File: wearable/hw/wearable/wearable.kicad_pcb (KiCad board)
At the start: 2 copper layers, 80.5 x 35.5 mm, 112 parts, among them IC1 LM4041CILPR, J2 Conn_02x05_Odd_Even, J8 USBC Charger, SW1 SW_Toggle, U1 LT3042xMSE, U2 BNO080, U3 nRF54L15-QFXX, U4 TPS61040DBV, U5 ADS1299IPAG, U6 nPM1300-QEXX, Y1 32MHz, Y2 32.768kHz, Y3 32.768kHz

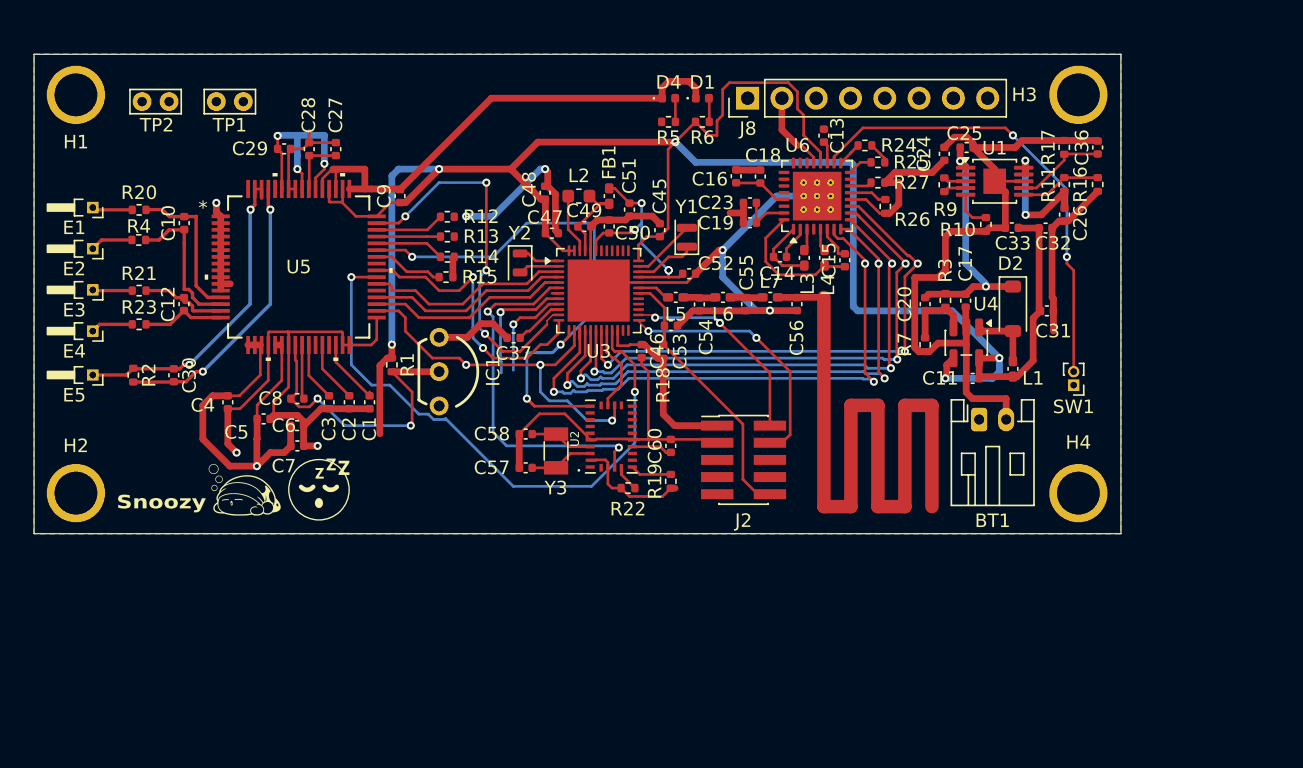
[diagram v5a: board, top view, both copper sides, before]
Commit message: Finished routing (mostly) + better testpoints
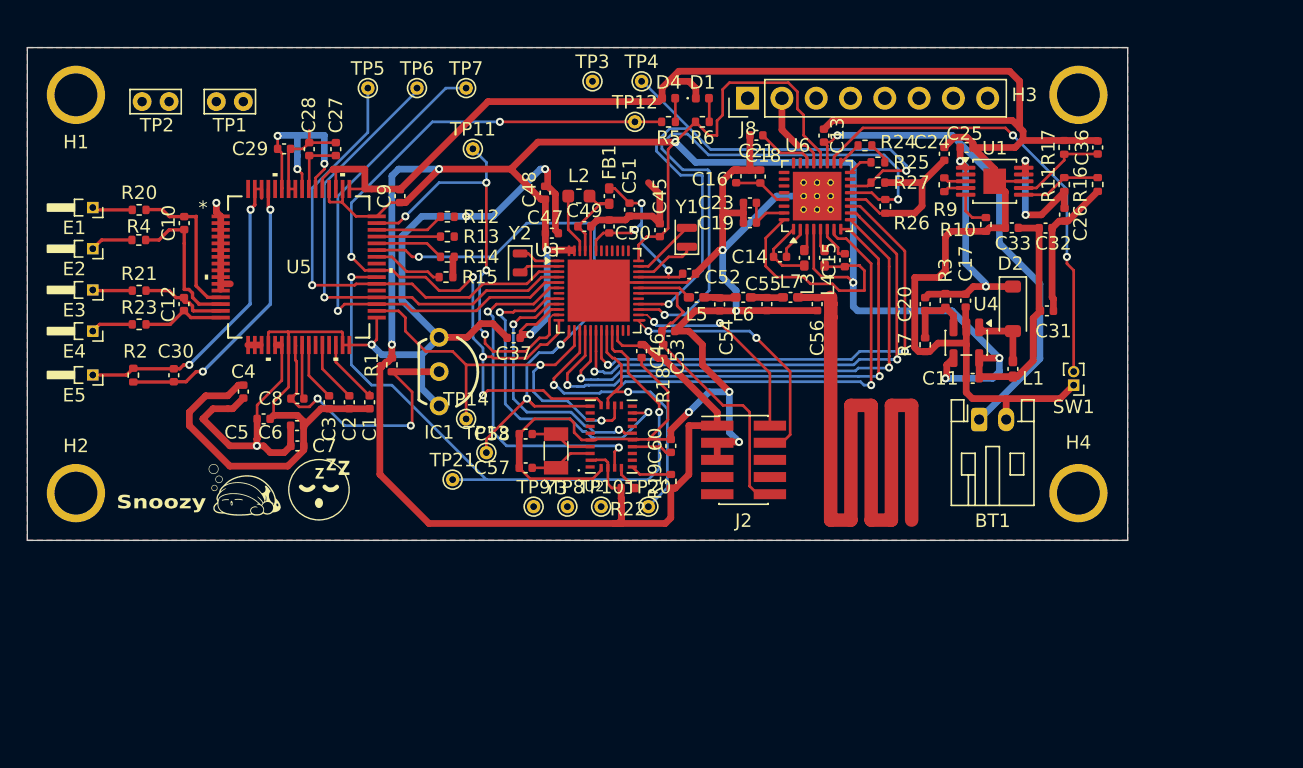
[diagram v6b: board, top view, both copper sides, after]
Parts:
- added C21: 1uF, Capacitor_SMD:C_0402_1005Metric, F.Cu at (163.0, 90.5)
- added TP10: TP, TestPoint:TestPoint_THTPad_D1.0mm_Drill0.5mm, F.Cu at (151.5, 118.0)
- added TP11: TP, TestPoint:TestPoint_THTPad_D1.0mm_Drill0.5mm, F.Cu at (142.0, 91.5)
- added TP12: TP, TestPoint:TestPoint_THTPad_D1.0mm_Drill0.5mm, F.Cu at (154.0, 89.5)
- added TP13: TP, TestPoint:TestPoint_THTPad_D1.0mm_Drill0.5mm, F.Cu at (143.0, 114.0)
- added TP14: TP, TestPoint:TestPoint_THTPad_D1.0mm_Drill0.5mm, F.Cu at (141.5, 111.5)
- added TP20: TP, TestPoint:TestPoint_THTPad_D1.0mm_Drill0.5mm, F.Cu at (155.0, 118.0)
- added TP21: TP, TestPoint:TestPoint_THTPad_D1.0mm_Drill0.5mm, F.Cu at (140.5, 116.0)
- added TP3: TP, TestPoint:TestPoint_THTPad_D1.0mm_Drill0.5mm, F.Cu at (150.9, 86.5)
- added TP4: TP, TestPoint:TestPoint_THTPad_D1.0mm_Drill0.5mm, F.Cu at (154.5, 86.5)
- added TP5: TP, TestPoint:TestPoint_THTPad_D1.0mm_Drill0.5mm, F.Cu at (134.2, 87.0)
- added TP6: TP, TestPoint:TestPoint_THTPad_D1.0mm_Drill0.5mm, F.Cu at (137.9, 87.0)
- added TP7: TP, TestPoint:TestPoint_THTPad_D1.0mm_Drill0.5mm, F.Cu at (141.5, 87.0)
- added TP8: TP, TestPoint:TestPoint_THTPad_D1.0mm_Drill0.5mm, F.Cu at (149.0, 118.0)
- added TP9: TP, TestPoint:TestPoint_THTPad_D1.0mm_Drill0.5mm, F.Cu at (146.5, 118.0)
- moved L5 1.54 mm to (158.6, 102.5)
- moved C54 1.50 mm to (160.3, 103.0)
- moved C55 1.50 mm to (163.8, 103.0)
- moved C56 1.50 mm to (167.5, 103.0)
- moved L6 1.50 mm to (162.0, 102.5)
- moved L7 1.50 mm to (165.5, 102.5)
- moved C4 1.40 mm to (125.0, 109.5), turned to 90 degrees
- moved C53 0.45 mm to (156.5, 105.0)
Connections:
- U3 pad 23: unconnected-(U3-P0.00-Pad23) -> SHPHLD
- U6 pad 22: unconnected-(U6-VBUSOUT-Pad22) -> Net-(U6-VBUSOUT)
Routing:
- net AVSS: track 244.9 -> 363.4 mm, vias 6 -> 8
- net +3V3: track 182.2 -> 231.8 mm, vias 5 -> 8
- net SCL: track 1.64 -> 47.7 mm, vias 0 -> 2
- net SCK: track 21.4 -> 65.8 mm, vias 2 -> 5
- net SDA: track 2.81 -> 44.4 mm, vias 0 -> 2
- net Net-(BT1-+): track 1.65 -> 37.0 mm, vias 0 -> 1
- net PWDWN_ADS1299: track 15.0 -> 39.0 mm, vias 0 -> 1
- net RST_ADS1299: track 14.9 -> 36.7 mm, vias 0 -> 1
- net START_ADS1299: track 15.3 -> 35.8 mm, vias 0 -> 1
- net INT_BNO085: track 9.29 -> 25.4 mm, vias 1 -> 2
- net CS_BNO085: track 6.50 -> 18.8 mm, vias 0 -> 1
- net RST_BNO085: track 7.39 -> 19.5 mm, vias 1 -> 2
- net AVDD: track 63.6 -> 55.7 mm
- net Net-(U6-VOUT2): track 10.3 -> 16.8 mm
- net CS_ADS1299: track 43.8 -> 49.5 mm
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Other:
- board size 80.5 x 35.5 mm -> 81.5 x 36.5 mm
- board text added: "Not sure if I can make these holes 0.3mm inner diameter (was 0.2)"

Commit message: Ready for review
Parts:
- removed TP20: TP, TestPoint:TestPoint_THTPad_D1.0mm_Drill0.5mm
- added R16: 10k, Resistor_SMD:R_0402_1005Metric, F.Cu at (171.0, 90.4)
- C32: renamed from C54; footprint Capacitor_SMD:C_0402_1005Metric -> Capacitor_SMD:C_0201_0603Metric
- C36: renamed from C55; footprint Capacitor_SMD:C_0402_1005Metric -> Capacitor_SMD:C_0201_0603Metric
- C38: renamed from C56; footprint Capacitor_SMD:C_0402_1005Metric -> Capacitor_SMD:C_0201_0603Metric
- L2: renamed from L5; footprint Inductor_SMD:L_0402_1005Metric_Pad0.77x0.64mm_HandSolder -> Inductor_SMD:L_0201_0603Metric
- L3: renamed from L6; footprint Inductor_SMD:L_0402_1005Metric_Pad0.77x0.64mm_HandSolder -> Inductor_SMD:L_0201_0603Metric
- L4: renamed from L7; footprint Inductor_SMD:L_0402_1005Metric_Pad0.77x0.64mm_HandSolder -> Inductor_SMD:L_0201_0603Metric
- SW1: footprint Connector_PinHeader_1.00mm:PinHeader_1x02_P1.00mm_Vertical -> Connector_PinHeader_1.27mm:PinHeader_1x02_P1.27mm_Vertical
- moved TP13 26.7 mm to (175.0, 98.0)
- moved TP12 11.5 mm to (145.0, 108.5)
- moved TP14 9.55 mm to (144.5, 90.5)
- moved TP10 8.90 mm to (143.5, 111.0)
- moved TP6 7.43 mm to (139.5, 115.5)
- moved C38 6.68 mm to (161.0, 101.6)
- moved L4 5.83 mm to (159.8, 101.3)
- moved C36 5.25 mm to (158.7, 101.6)
- moved L3 4.61 mm to (157.6, 101.3)
- moved C32 4.54 mm to (156.1, 101.3), turned to 180 degrees
- moved R27 3.82 mm to (184.8, 95.6)
- moved TP5 3.61 mm to (137.5, 114.0)
- moved R12 2.65 mm to (157.0, 104.0), turned to 0 degrees
- moved L2 2.56 mm to (156.0, 102.1)
- moved C48 2.50 mm to (186.8, 93.4)
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- renumbered C10 to C1, C27 to C10, C2 to C11, C3 to C12, C7 to C13, C9 to C14, C1 to C15, C58 to C16, C57 to C17, C37 to C18, C48 to C19, C12 to C2, C47 to C20, C49 to C21, C51 to C22, C45 to C23, C50 to C24, C46 to C25, C60 to C26, C53 to C27, C16 to C28, C19 to C29, C30 to C3, C23 to C30, C52 to C31, C21 to C33, C18 to C34, C14 to C35, C15 to C37, C13 to C39, C29 to C4, C24 to C40, C20 to C41, C25 to C42, C17 to C43, C11 to C44, C33 to C45, C32 to C46, C31 to C47, C36 to C48, C26 to C49, C4 to C5, C5 to C6, C8 to C7, C6 to C8, C28 to C9, D4 to D1, D1 to D2, D2 to D3, J8 to J1, L2 to L1, L3 to L5, L4 to L6, L1 to L7, R20 to R1, R15 to R10, R22 to R11, R18 to R12, R19 to R13, R5 to R14, R6 to R15, R24 to R17, R25 to R18, R27 to R19, R4 to R2, R26 to R20, R7 to R21, R10 to R22, R9 to R23, R3 to R24, R17 to R25, R11 to R26, R16 to R27, R21 to R3, R23 to R4, R2 to R5, R1 to R6, R12 to R7, R13 to R8, R14 to R9, TP2 to TP1, TP8 to TP10, TP13 to TP11, TP10 to TP12, TP3 to TP13, TP12 to TP14, TP4 to TP15, TP1 to TP2, TP5 to TP3, TP6 to TP4, TP21 to TP5, TP9 to TP6, TP11 to TP8, TP14 to TP9, U5 to U1, U3 to U2, U2 to U3, U6 to U4, U1 to U5, U4 to U6, Y2 to Y1, Y3 to Y2, Y1 to Y3
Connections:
- J1 pad 4: unconnected-(J8-Pin_4-Pad4) -> Net-(J1-Pin_4)
- J1 pad 8: unconnected-(J8-Pin_8-Pad8) -> Net-(J1-Pin_8)
- R17 pad 2: Net-(R24-Pad2) -> AVSS
- R18 pad 2: Net-(R24-Pad2) -> AVSS
- SW1 pad 2: Net-(U6-NTC) -> Net-(U4-SHPHLD)
- U2 pad 23: SHPHLD -> unconnected-(U2-P0.00-Pad23)
- U4 pad 15: SHPHLD -> Net-(U4-SHPHLD)
- U4 pad 18: Net-(U6-NTC) -> Net-(U4-NTC)
- U4 pad 23: CC1 -> Net-(J1-Pin_4)
- U4 pad 24: CC2 -> Net-(J1-Pin_8)
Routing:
- net AVSS: track 363.4 -> 292.7 mm, vias 8 -> 19
- net SCL: track 47.7 -> 88.5 mm, vias 2 -> 4
- net Net-(J1-Pin_8): track 0.00 -> 37.7 mm, vias 0 -> 1
- net Net-(U6-NTC): track 34.2 -> 0.00 mm, vias 2 -> 0
- net Net-(U4-SHPHLD): track 0.00 -> 32.9 mm, vias 0 -> 1
- net RF: track 59.9 -> 36.9 mm
- net GPIO2: track 38.9 -> 56.7 mm
- net GPIO1: track 40.5 -> 57.5 mm
- net GPIO3: track 38.5 -> 55.2 mm
- net GPIO4: track 38.1 -> 54.7 mm
- net GPIO0: track 42.1 -> 58.2 mm
- net AVDD: track 55.7 -> 39.9 mm, vias 7 -> 9
- net SDA: track 44.4 -> 59.6 mm
- net CS_BNO085: track 18.8 -> 6.50 mm, vias 1 -> 0
- net Net-(J1-Pin_4): track 0.00 -> 8.38 mm, vias 0 -> 1
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- added copper zone on In2.Cu, net AVDD
- added copper zone on In1.Cu, net AVSS
- removed copper zone on B.Cu, net AVDD
- removed copper zone on F.Cu, net AVSS
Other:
- board size 81.5 x 36.5 mm -> 81.5 x 38 mm
- copper layers 2 -> 4

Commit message: Gerbers
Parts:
- added G***: LOGO, LOGO, B.Cu at (181.3, 117.4)
- moved TP13 14.2 mm to (175.4, 112.2)
- moved TP11 5.40 mm to (137.6, 114.2)
- moved TP6 2.75 mm to (139.5, 112.8)
- moved TP5 2.51 mm to (137.2, 111.5)
- moved G*** 1.35 mm to (125.1, 118.1)
- moved TP7 1.10 mm to (139.9, 88.0)
- moved G*** 0.95 mm to (130.6, 117.7)
- moved TP3 0.40 mm to (134.9, 88.0)
- turned C5 to -90 degrees
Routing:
- net AVSS: track 292.7 -> 242.9 mm, vias 19 -> 17
- net AVDD: track 39.9 -> 46.4 mm, vias 9 -> 8
- net MISO: track 45.5 -> 51.0 mm
- net Net-(U1-VREFP): track 22.6 -> 17.8 mm
- net +5V3: track 18.9 -> 23.5 mm
- net +3V3: track 229.6 -> 225.1 mm, vias 13 -> 9
- net Net-(J1-Pin_8): track 37.7 -> 33.4 mm
- net GPIO4: track 54.7 -> 58.2 mm
- net Net-(U1-BIASINV): track 23.8 -> 20.7 mm, vias 2 -> 0
- net Net-(U1-BIASIN): track 25.4 -> 23.4 mm, vias 2 -> 0
- net GPIO3: track 55.2 -> 57.1 mm
- net CS_ADS1299: track 48.1 -> 46.6 mm
- net PWDWN_ADS1299: track 37.1 -> 35.6 mm
- net Net-(U4-VOUT2): track 12.1 -> 13.3 mm
- net INT_BNO085: track 33.0 -> 31.9 mm
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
